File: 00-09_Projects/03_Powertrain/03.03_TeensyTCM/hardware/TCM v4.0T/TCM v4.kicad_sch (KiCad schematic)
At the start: 32 parts, among them J2 Conn_02x06_Counter_Clockwise, U2 SN65HVD230, U3 TPS62933, U4 SN65HVD230

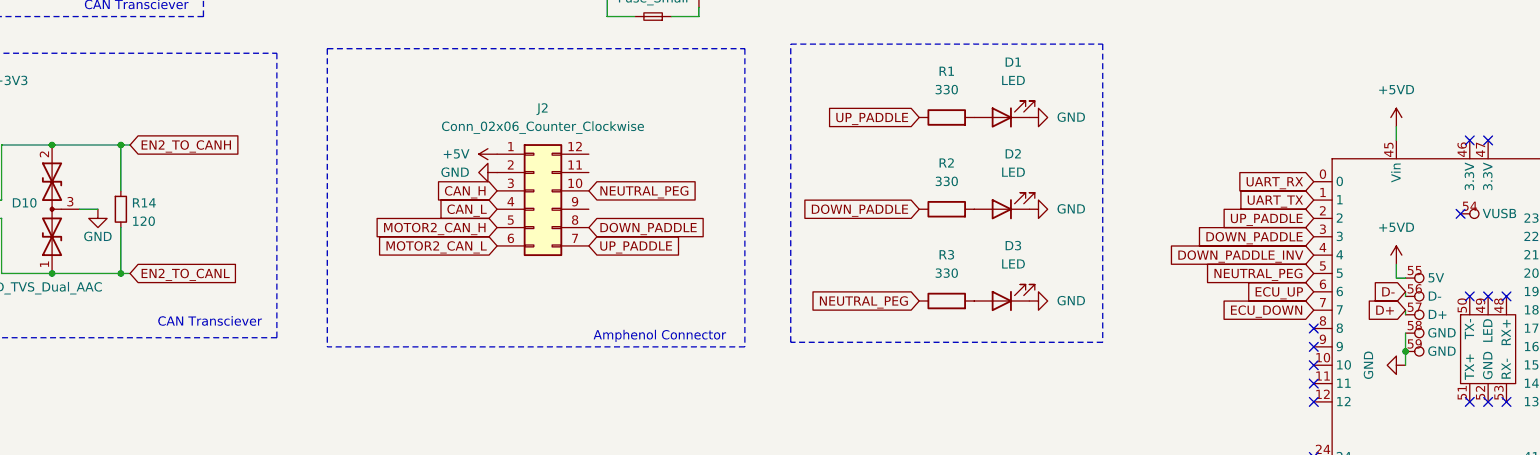
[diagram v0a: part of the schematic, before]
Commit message: teensy label fixes
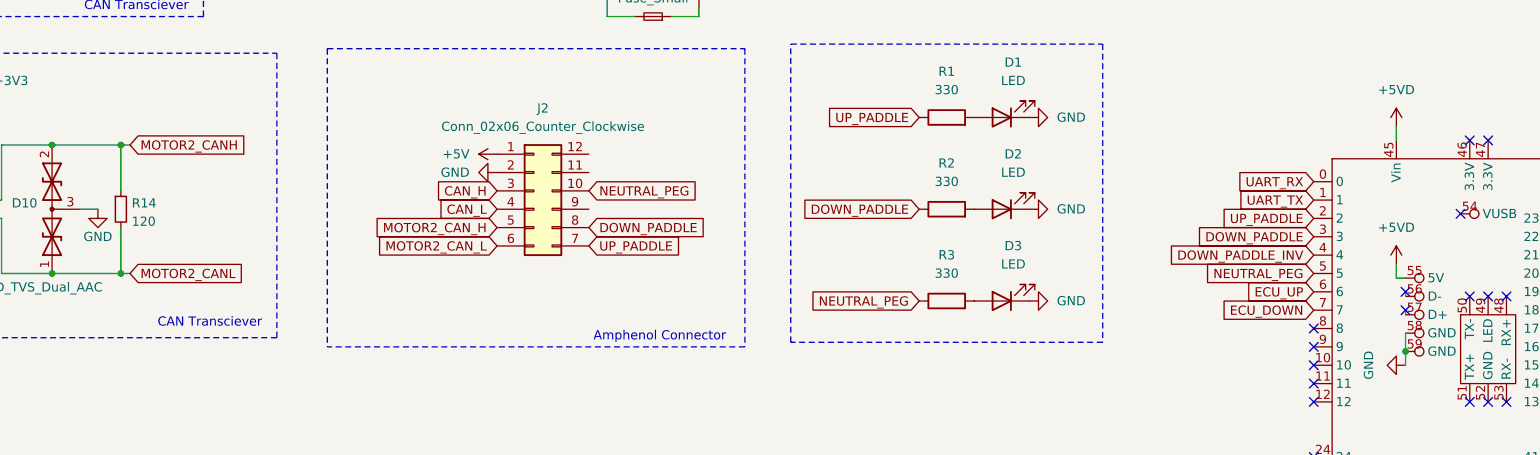
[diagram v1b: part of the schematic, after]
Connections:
- net D+: no longer names the net of U1.57 (D+)
- net D-: no longer names the net of U1.56 (D-)
- net EN2_TO_CANH renamed MOTOR2_CANH
- net EN2_TO_CANL renamed MOTOR2_CANL
- no-connect marks 50 -> 52

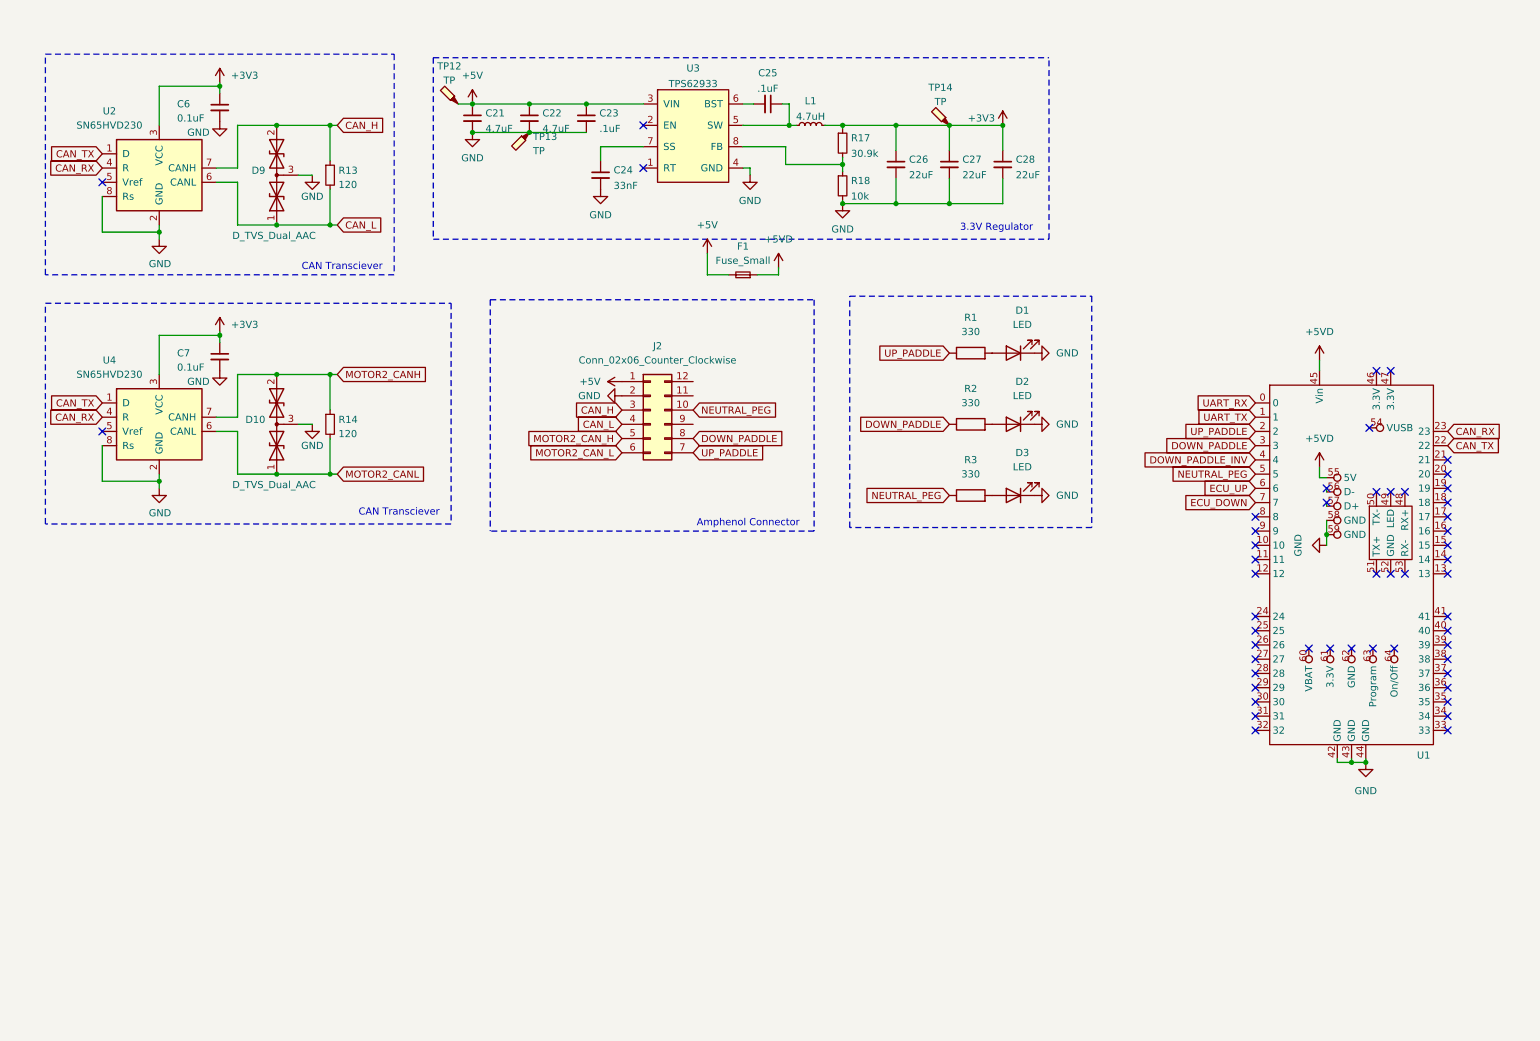
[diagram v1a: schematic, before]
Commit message: implemented all design review 1 changes
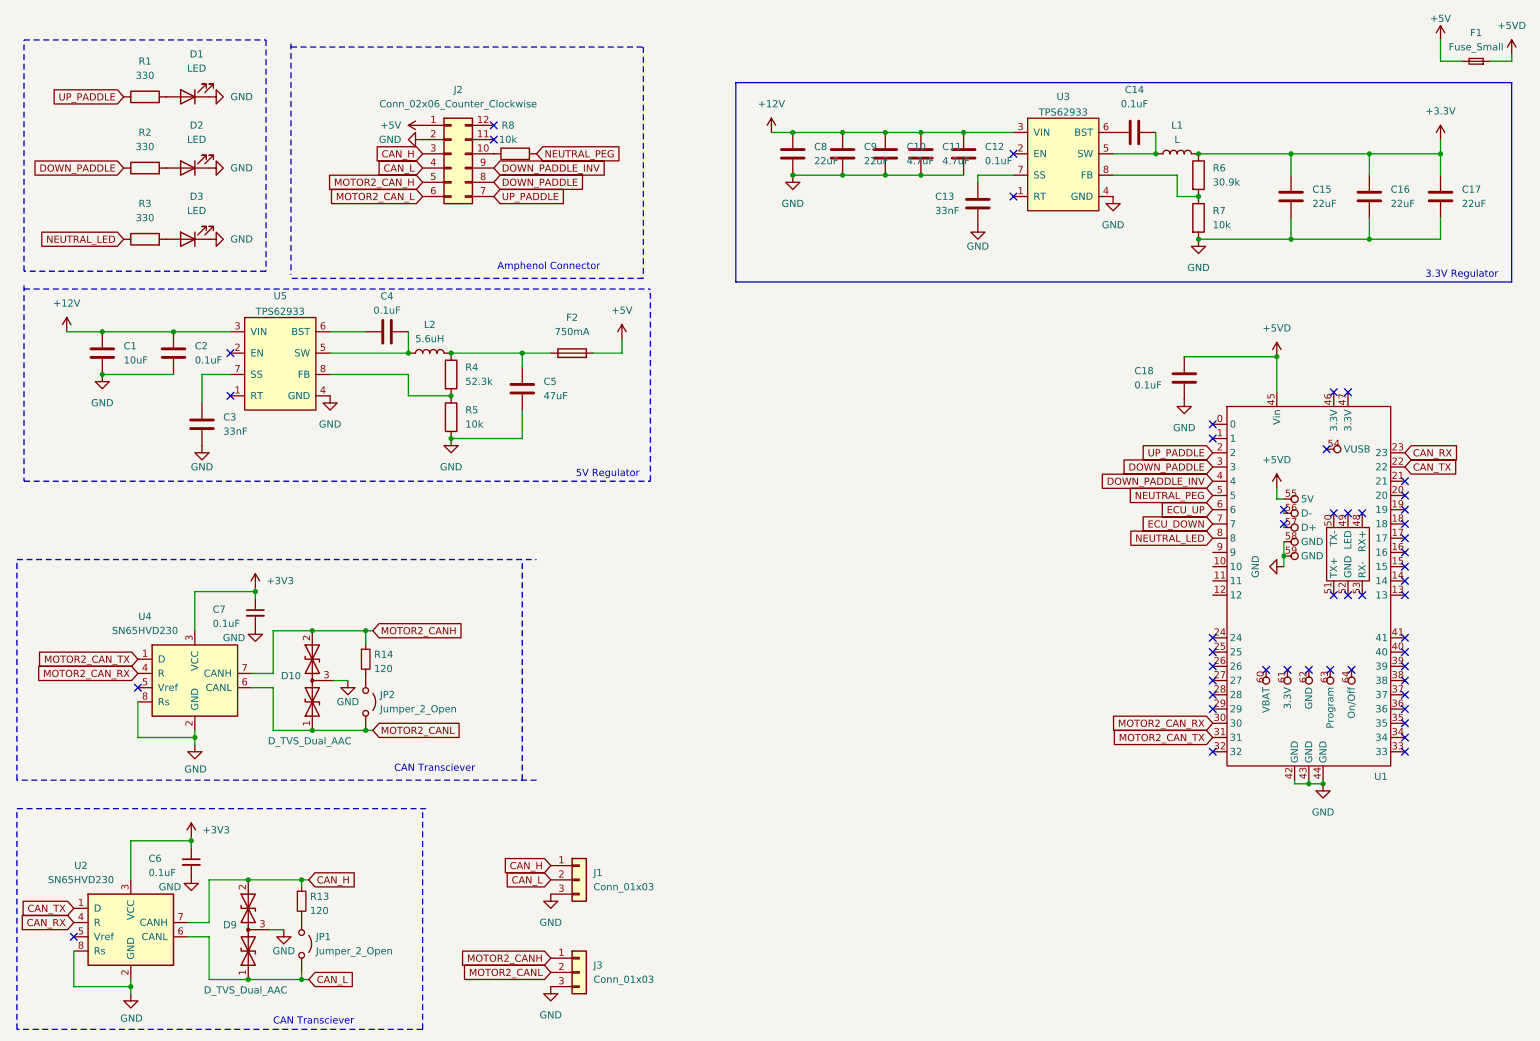
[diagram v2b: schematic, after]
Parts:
- removed C21, C22: 4.7uF, Capacitor_SMD:C_0805_2012Metric, symbol Device:C_Small
- removed C23, C25: .1uF, Capacitor_SMD:C_0603_1608Metric, symbol Device:C_Small
- removed C24: 33nF, Capacitor_SMD:C_0603_1608Metric, symbol Device:C_Small
- removed C26, C27, C28: 22uF, Capacitor_SMD:C_0805_2012Metric, symbol Device:C_Small
- removed L1: 4.7uH, LHR:SRU8043-4R7Y, symbol Device:L_Small
- removed R17: 30.9k, Resistor_SMD:R_0603_1608Metric, symbol Device:R_Small
- removed R18: 10k, Resistor_SMD:R_0603_1608Metric, symbol Device:R_Small
- removed TP12, TP13, TP14: TP, TestPoint:TestPoint_Pad_D2.0mm, symbol Connector:TestPoint_Probe
- added C1: 10uF, symbol Device:C
- added C10, C11: 4.7uF, symbol Device:C
- added C12, C14, C18, C2, C4: 0.1uF, symbol Device:C
- added C13, C3: 33nF, symbol Device:C
- added C15, C16, C17, C8, C9: 22uF, symbol Device:C
- added C5: 47uF, symbol Device:C
- added F2: 750mA, Package_SO:SSOP-20_3.9x8.7mm_P0.635mm, symbol Device:Fuse
- added J1, J3: Conn_01x03, Connector_PinHeader_2.54mm:PinHeader_1x03_P2.54mm_Vertical, symbol Connector_Generic:Conn_01x03
- added JP1, JP2: Jumper_2_Open, symbol Jumper:Jumper_2_Open
- added L1: L, Package_SO:SOIC-16_3.9x9.9mm_P1.27mm, symbol Device:L
- added L2: 5.6uH, Package_SO:SOIC-16_3.9x9.9mm_P1.27mm, symbol Device:L
- added R4: 52.3k, symbol Device:R
- added R5, R7, R8: 10k, symbol Device:R
- added R6: 30.9k, symbol Device:R
- added U5: TPS62933, LHR:SOT-583, symbol LHR:TPS62933
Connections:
- net +5V: now also F2.2; no longer U3.3 (VIN)
- net +5VD: now also C18.1
- net CAN_H: now also J1.1 (Pin_1)
- net CAN_L: now also J1.2 (Pin_2), JP1.2 (B); no longer R13.2
- net CAN_RX: no longer U4.4 (R)
- net CAN_TX: no longer U4.1 (D)
- net DOWN_PADDLE_INV: now also J2.9 (Pin_9)
- net GND: now also C1.2, C10.2, C11.2, C12.2, C13.2, C15.2, C16.2, C17.2, C18.2, C2.2, C3.2, C5.2, C8.2, C9.2, J1.3 (Pin_3), J3.3 (Pin_3), R5.2, R7.2, U5.4 (GND)
- net MOTOR2_CANH: now also J3.1 (Pin_1)
- net MOTOR2_CANL: now also J3.2 (Pin_2), JP2.2 (B); no longer R14.2
- net NEUTRAL_PEG: now also R8.2; no longer J2.10 (Pin_10), R3.1
- net at U3.5 (SW): now also C14.2, L1.1
- net at U3.6 (BST): now also C14.1
- net at U3.7 (SS): now also C13.1
- net at U3.8 (FB): now also R6.2, R7.1
- net MOTOR2_CAN_RX: now reaches U1.30
- net MOTOR2_CAN_RX: now also U4.4 (R)
- net MOTOR2_CAN_TX: now reaches U1.31
- net MOTOR2_CAN_TX: now also U4.1 (D)
- net NEUTRAL_LED: now reaches U1.8
- net NEUTRAL_LED: now also R3.1
- net UART_RX: no longer names the net of U1.0
- net UART_TX: no longer names the net of U1.1
- new net: C4.1, U5.6 (BST)
- new net: C4.2, L2.1, U5.5 (SW)
- new net: J2.10 (Pin_10), R8.1
- new net: C3.1, U5.7 (SS)
- new net: R4.2, R5.1, U5.8 (FB)
- new net: C5.1, F2.1, L2.2, R4.1
- new net: JP2.1 (A), R14.2
- new net: JP1.1 (A), R13.2
- new net +12V: C1.1, C10.1, C11.1, C12.1, C2.1, C8.1, C9.1, U3.3 (VIN), U5.3 (VIN)
- new net +3.3V: C15.1, C16.1, C17.1, L1.2, R6.1
- no-connect marks 52 -> 51
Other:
- note added: "5V Regulator"
- moved on the sheet: C6, C7, D1, D10, D2, D3, D9, F1, J2, R1, R13, R14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
